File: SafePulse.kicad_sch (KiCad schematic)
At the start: 86 parts, among them IC1 S-35770E01I-K8T2U, J1 Conn_01x03_Male, J2 4208, Q1 FQT7N10L, Q2 BC846A, Q3 MMBT3906, Q4 MMBT3906, U1 TS4061AICT-1.25, U2 74HC14, U33 MAX9910EXK+T, U4 CD14538BM

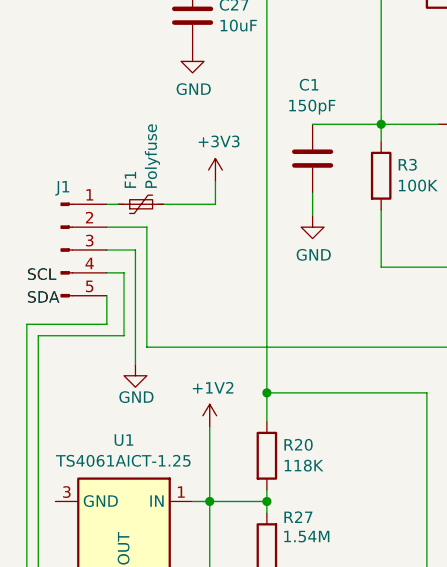
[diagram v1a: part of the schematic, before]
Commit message: Aligned labels on board and replaces text labels in schematics
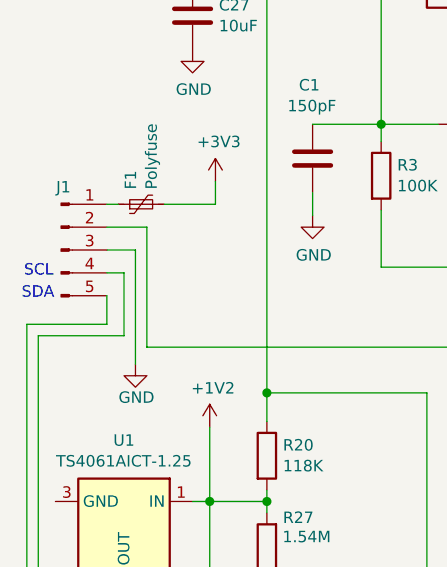
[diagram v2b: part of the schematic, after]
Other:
- note added: "SCL"
- note added: "SDA"

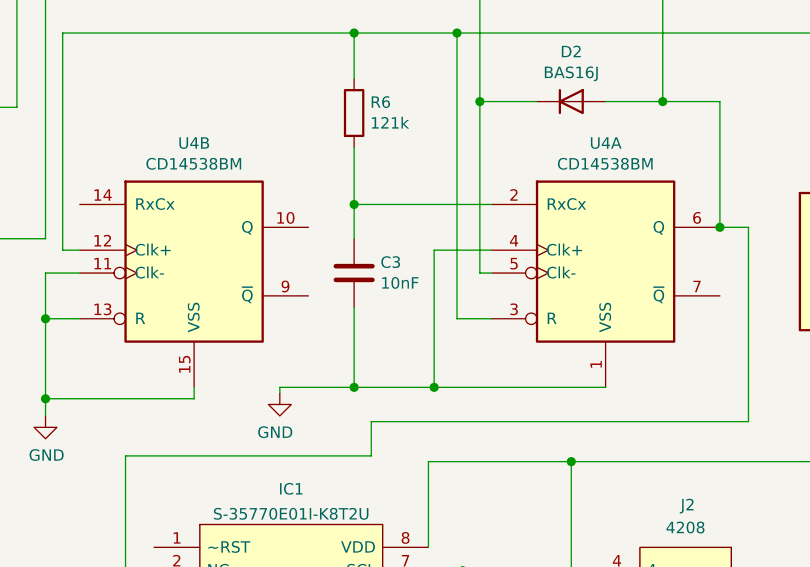
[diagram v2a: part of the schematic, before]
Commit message: V1.2.6  with update BOM and C3 to 1nf
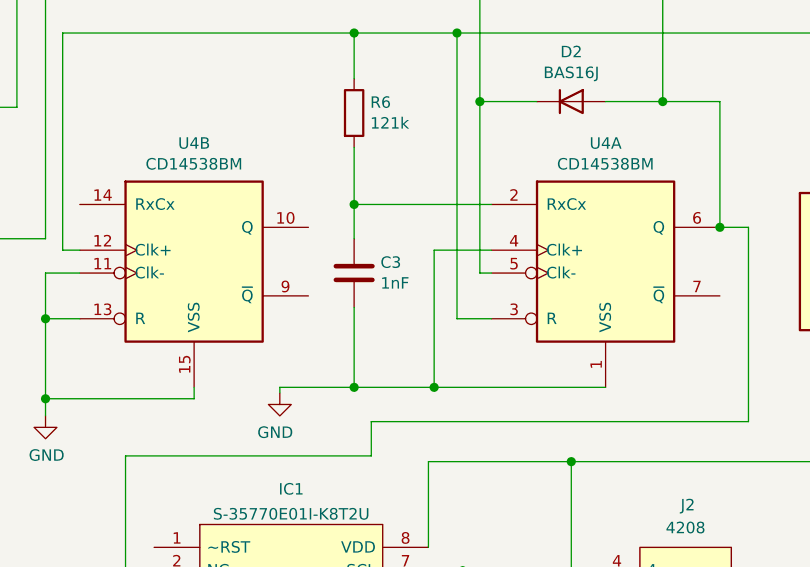
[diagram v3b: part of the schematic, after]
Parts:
- C3: value 10nF -> 1nF; LCSC C83170 -> C94121; LCSC Part # C83170 -> C94121
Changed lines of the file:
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@@
 	(title_block
 		(title "SafePulse High Voltage Geiger Muller Power Supply")
-		(date "2025-04-05")
+		(date "2025-04-12")
 		(rev "1.2.6")
 		(company "SafeCast Team")
@@
 			)
 		)
-		(property "Value" "10nF"
+		(property "Value" "1nF"
 			(at 104.521 150.368 0)
 			(effects
@@
 			)
 		)
-		(property "Datasheet" "https://www.digikey.com/en/products/detail/avx-corporation/08055C102KAT2A/563481"
+		(property "Datasheet" "https://www.lcsc.com/datasheet/lcsc_datasheet_1810311439_YAGEO-CC0805KRX7R9BB102_C94121.pdf"
 			(at 101.6 149.225 0)
 			(effects
@@
 			)
 		)
-		(property "LCSC Part #" "C83170"
+		(property "LCSC Part #" " C94121"
 			(at 101.6 149.225 0)
 			(effects
@@
 			)
 		)
-		(property "LCSC" "C83170"
+		(property "LCSC" " C94121"
 			(at 104.521 148.0566 0)
 			(effects

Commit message: Cleaned up files . JLCPCB production files generated for V2.0.0
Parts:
- added C20: 100pF, Capacitor_SMD:C_0805_2012Metric, symbol Device:C
- added C21: 0.1uF, Capacitor_SMD:C_0805_2012Metric, symbol Device:C
- added R2: 10M, Resistor_SMD:R_1206_3216Metric, symbol Device:R
- added R26: 22M, Resistor_SMD:R_0805_2012Metric, symbol Device:R
- C1: value 150pF -> 110pF; Digikey 732-12190-1-ND -> 3372-0805B101K101BDTR-ND; LCSC C520084 -> C17694684; LCSC Part # C520084 -> C17694684
- C22: value 1.5nF -> 390pF; LCSC C1717 -> C1741; LCSC Part # C1717 -> C1741
- C4: value 10uF -> 47uF; LCSC C1713 -> C76636; LCSC Part # C1713 -> C76636
- H1, J1, two_pinheader1: now left out of the parts list
- H2: value Anode -> LND712; now left out of the parts list
- H4: value Anode -> LND7317; now left out of the parts list
- J2: value 4208 -> JST SM04B-SRSS-TB(LF)(SN); LCSC Part # (none) -> C160404
- R17: LCSC C317482 -> C17721; LCSC Part # C317482 -> C17721
- R22: value 12K -> 20K; LCSC C17444 -> C2988970; LCSC Part # C17444 -> C2988970
- R24: value 22k -> 33k; Digikey CR0805-FX-2202ELFCT-ND -> A129767CT-ND; LCSC C352242 -> C17633; LCSC Part # C352242 -> C17633
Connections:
- net +3V3: now also IC1.1 (~RST), C21.2
- net GND: now also U4.12 (Clk+), U4.14 (RxCx), C21.1; no longer C3.2, U4.1 (VSS), U4.11 (Clk-), U4.13 (R), U4.15 (VSS)
- net at C18.2, D9.2 (A), D9.3 (K)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: now also R2.1
- net at C23.1, R12.2, R6.1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: now also U4.11 (Clk-), U4.13 (R); no longer U4.12 (Clk+)
- net at R23.1, R7.1, U33.3 (-): now also R26.1
- net at R3.2, TP2.1, U33.4: now also C20.2
- net at H4.1, R1.2: no longer H2.1
- new net: C3.2, U4.1 (VSS)
- new net: H2.1, R2.2
- new net: C20.1, R26.2
- no-connect marks 0 -> 3
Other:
- note added: "Anode"
- title: SafePulse High Voltage Geiger Muller Power Supply -> SafePulse High Voltage Geiger-Muller Power Supply
- moved on the sheet: D2, IC1, J2, R1, R12, R23, R24, U33, U4A, U4B
